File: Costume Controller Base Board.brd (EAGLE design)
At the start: 100 x 80 mm, 33 parts, among them J1 USB MICRO, U1 ATMEGA32U4-XUMU, U3 LP2985-33DBVR, U4 MPU-6050-1, U5 TPS61200, Y1 16MHz KX-7

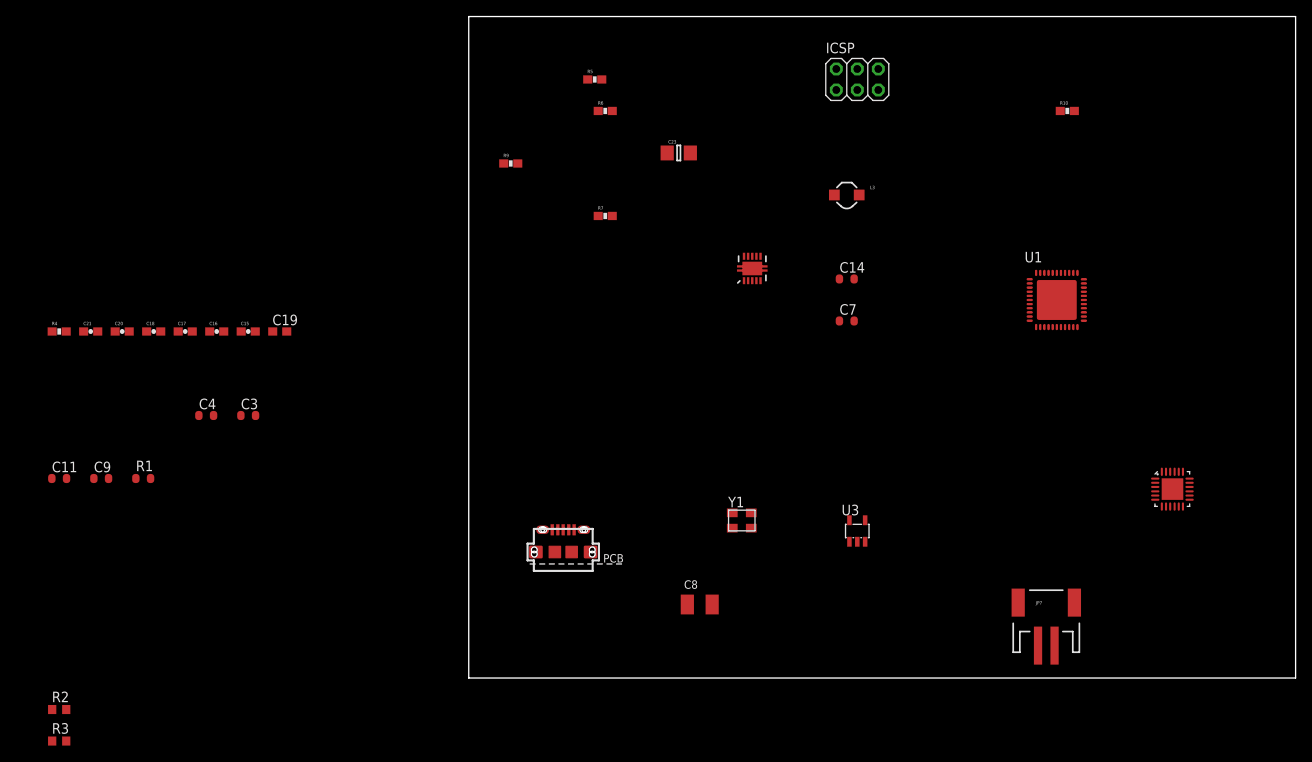
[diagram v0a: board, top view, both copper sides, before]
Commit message: complete schematic, though VUSB needs further study, probably won't power +5v
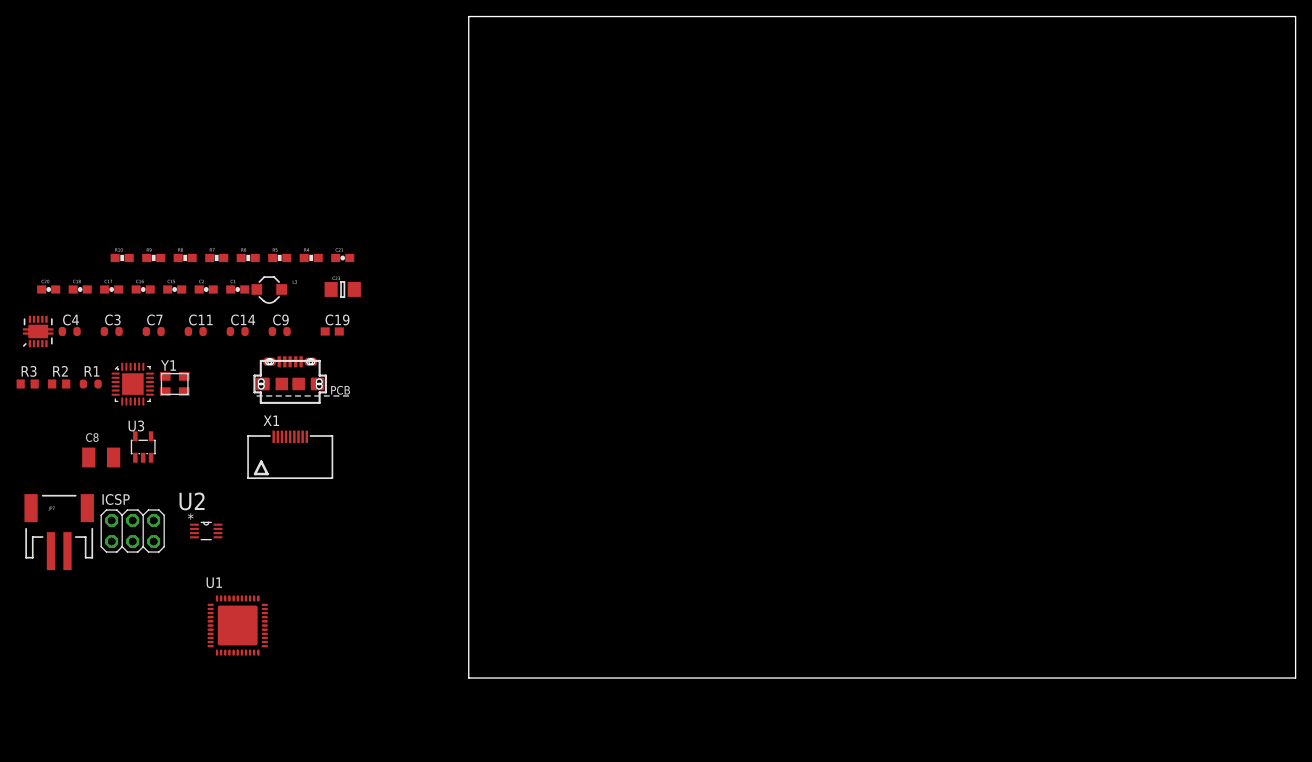
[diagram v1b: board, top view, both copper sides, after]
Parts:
- added C1, C2: 0.1uF, SparkFun:0603-CAP
- added R8: 10k, SparkFun:0603-RES
- added U2: PCA9306DCUT, Texas Instruments_By_element14_Batch_1:SOP50P310X90-8N
- added X1: 09FLZ-SM1, con-jst:9FLZ-SM
- moved U4 126.4 mm to (-40.6, 35.6)
- moved JP7 119.9 mm to (-49.5, 19.1)
- moved R10 115.7 mm to (-41.9, 50.8)
- moved U1 106.6 mm to (-27.9, 6.35)
- moved ICSP 103.3 mm to (-40.6, 17.8)
- moved U3 87.0 mm to (-39.4, 27.9)
- moved U5 86.7 mm to (-52.1, 41.9)
- moved C7 83.8 mm to (-38.1, 41.9)
- moved C8 74.5 mm to (-44.5, 26.7)
- moved C14 73.9 mm to (-27.9, 41.9)
- moved L3 70.8 mm to (-24.1, 47.0)
- moved Y1 70.5 mm to (-35.6, 35.6)
- moved R7 47.3 mm to (-30.5, 50.8)
- moved R6 46.7 mm to (-26.7, 50.8)
- moved R9 44.7 mm to (-38.1, 50.8)
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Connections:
- removed net SCL: R4.1, U1.18, U4.23
- removed net SDA: R5.1, U1.19, U4.24
- new net N$15: U1.8
- new net N$2: C2.1, R8.1
- new net SCL2: U1.18
- new net SDA1: U4.24
- new net SDA2: U1.19
- new net STRAND1: U1.20, X1.1
- new net STRAND2: U1.21
- new net STRAND3: U1.25
- new net STRAND4: U1.22, X1.4
- new net STRAND5: U1.26, X1.5
- new net STRAND6: U1.27, X1.6
- new net STRAND7: U1.33, X1.7
- new net STRAND8: U1.31
- new net STRAND9: U1.32, X1.9
- new net VREF1: U2.2
- new net VREF2: U2.7
- net +3V3: now also C1.1
- net +5V: now also R8.2
- net GND: now also C1.2, C2.2
- net INT: now also U1.1

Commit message: Draft, proofreading required, some components need package changes or value confirmation, board layout and routing required.
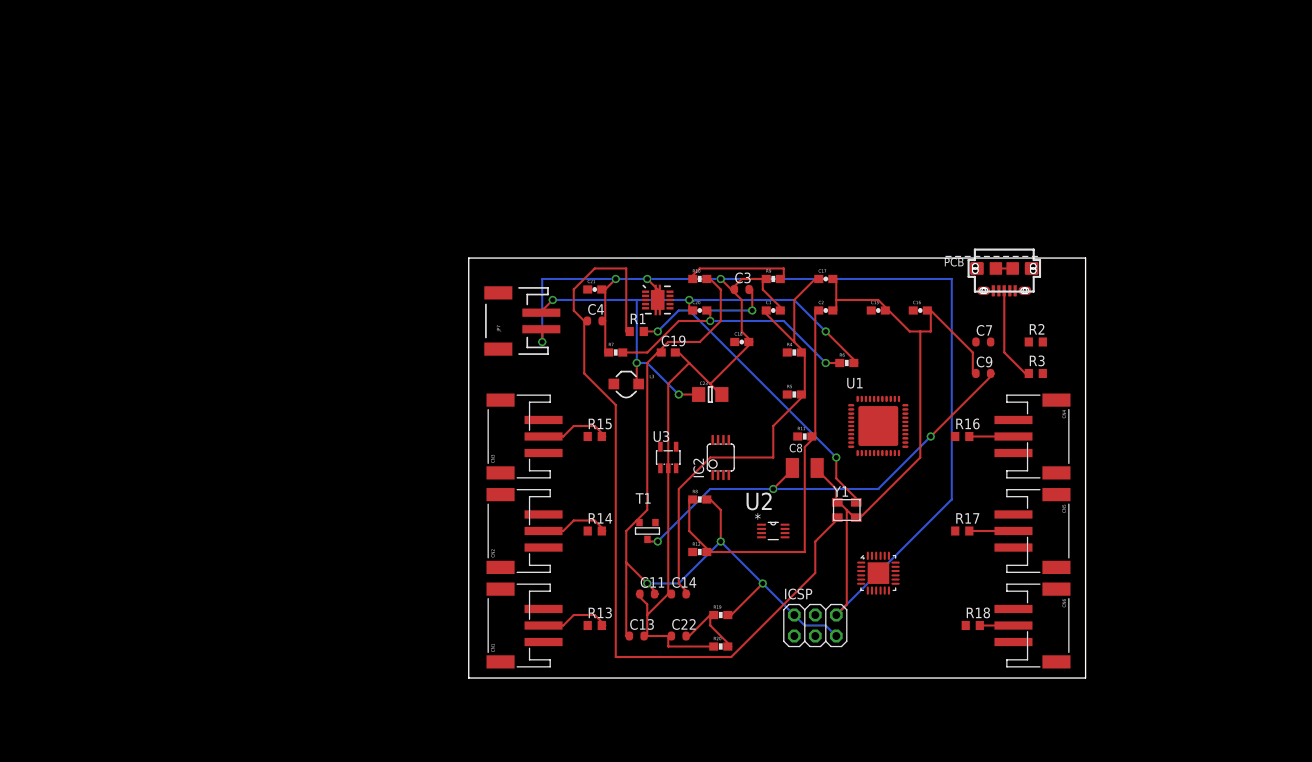
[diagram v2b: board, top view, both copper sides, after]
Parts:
- removed X1: 09FLZ-SM1, con-jst:9FLZ-SM
- added C13, C22: 100n, SmartPrj:C0603-ROUND
- added CN1, CN2, CN3, CN4, CN5, CN6: (no value), adafruit:JSTPH3
- added IC2: LMV358IDGKR, linear:MSOP08
- added R11, R12, R19, R20: 10k, SparkFun:0603-RES
- added R13, R14, R15, R16, R17, R18: 300, resistor:R0603
- added T1: FDN340P, zetex:SOT-23
- R1: device SmartPrj:R0603-ROUND -> resistor:R0603
- moved R3 121.9 mm to (68.6, 36.8)
- moved R2 118.2 mm to (68.6, 40.6)
- moved C7 100.3 mm to (62.2, 40.6)
- moved C16 94.0 mm to (54.6, 44.5)
- moved U4 93.0 mm to (49.5, 12.7)
- moved J1 87.5 mm to (64.8, 49.5), turned to 180 degrees
- moved C17 86.4 mm to (43.2, 48.3)
- moved C9 85.2 mm to (62.2, 36.8)
- moved C15 85.1 mm to (49.5, 44.5)
- moved C8 85.1 mm to (40.6, 25.4)
- moved ICSP 83.3 mm to (41.9, 6.35)
- moved Y1 82.7 mm to (45.7, 20.3)
- moved U1 81.1 mm to (49.5, 30.5)
- moved C18 80.3 mm to (33.0, 40.6)
- moved C20 78.8 mm to (27.9, 44.5)
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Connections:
- removed net AUX_SCL: U4.7
- removed net AUX_SDA: U4.6
- removed net GND3: U1.43
- removed net N$15: U1.8
- removed net STRAND7: U1.33, X1.7
- removed net STRAND8: U1.31
- removed net STRAND9: U1.32, X1.9
- removed net VREF1: U2.2
- removed net VREF2: U2.7
- new net CMP: C22.2, IC2.5, R19.1, R20.2
- new net GATE_CMD: IC2.7, T1.3
- new net N$10: CN2.2, R14.2
- new net N$11: CN1.2, R13.2
- new net N$3: CN6.2, R18.2
- new net N$6: CN5.2, R17.2
- new net N$7: CN4.2, R16.2
- new net N$8: CN3.2, R15.2
- new net SCL1: R4.1, U2.3, U4.23
- net +3V3: now also IC2.6, U2.2
- net +5V: now also C13.1, CN1.1, CN2.1, CN3.1, CN4.1, CN5.1, CN6.1, IC2.8, R19.2, T1.2
- net GND: now also C13.2, C22.1, CN1.3, CN2.3, CN3.3, CN4.3, CN5.3, CN6.3, IC2.4, R20.1, U1.43, U2.1
- net N$2: now also R11.2, R12.2, U2.7, U2.8
- net SCL2: now also R11.1, U2.6
- net SDA1: now also R5.1, U2.4
- net SDA2: now also R12.1, U2.5
- net STRAND1: now also R13.1; no longer X1.1
- net STRAND2: now also R14.1
- net STRAND3: now also R15.1
- net STRAND4: now also R16.1; no longer X1.4
- net STRAND5: now also R17.1; no longer X1.5
- net STRAND6: now also R18.1; no longer X1.6
- net VUSB: now also T1.1
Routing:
- net GND: track 0.00 -> 285.2 mm, vias 0 -> 4
- net +5V: track 0.00 -> 99.6 mm, vias 0 -> 3
- net XTAL1: track 0.00 -> 98.5 mm
- net VIN: track 0.00 -> 63.8 mm, vias 0 -> 5
- net +3V3: track 0.00 -> 58.4 mm
- net VUSB: track 0.00 -> 54.8 mm, vias 0 -> 3
- net N$2: track 0.00 -> 50.2 mm
- net XTAL2: track 0.00 -> 48.7 mm, vias 0 -> 3
- net UVLO: track 0.00 -> 31.6 mm, vias 0 -> 2
- net FB: track 0.00 -> 14.1 mm
- net D+: track 0.00 -> 11.6 mm
- net CMP: track 0.00 -> 9.68 mm
- net N$8: track 0.00 -> 8.93 mm
- net N$11: track 0.00 -> 8.93 mm
- net N$10: track 0.00 -> 8.93 mm
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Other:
- board size 100 x 80 mm -> 74.6 x 50.8 mm
